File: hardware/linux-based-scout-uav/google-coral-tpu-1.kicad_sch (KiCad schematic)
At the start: 1 part, among them U10 G313-06329-00

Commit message: Schematic and board update
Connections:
- net USB_2_DP: now reaches U10.13 (USB2_D_P)
- net USB_2_DN: now reaches U10.14 (USB2_D_N)
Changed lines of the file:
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@@
+	(wire
+		(pts
+			(xy 168.91 142.24) (xy 180.34 142.24)
+		)
+		(stroke
+			(width 0)
+			(type default)
+		)
+	)
 	(wire
 		(pts
@@
 		)
 	)
+	(wire
+		(pts
+			(xy 168.91 139.7) (xy 180.34 139.7)
+		)
+		(stroke
+			(width 0)
+			(type default)
+		)
+	)
+	(global_label "USB_2_DN"
+		(shape bidirectional)
+		(at 168.91 142.24 180)
+		(fields_autoplaced yes)
+		(effects
+			(font
+				(size 1.27 1.27)
+			)
+			(justify right)
+		)
+		(property "Intersheetrefs" "${INTERSHEET_REFS}"
+			(at 155.2583 142.24 0)
+			(effects
+				(font
+					(size 1.27 1.27)
+				)
+				(justify right)
+				(hide yes)
+			)
+		)
+	)
+	(global_label "USB_2_DP"
+		(shape bidirectional)
+		(at 168.91 139.7 180)
+		(fields_autoplaced yes)
+		(effects
+			(font
+				(size 1.27 1.27)
+			)
+			(justify right)
+		)
+		(property "Intersheetrefs" "${INTERSHEET_REFS}"
+			(at 155.3188 139.7 0)
+			(effects
+				(font
+					(size 1.27 1.27)
+				)
+				(justify right)
+				(hide yes)
+			)
+		)
+	)

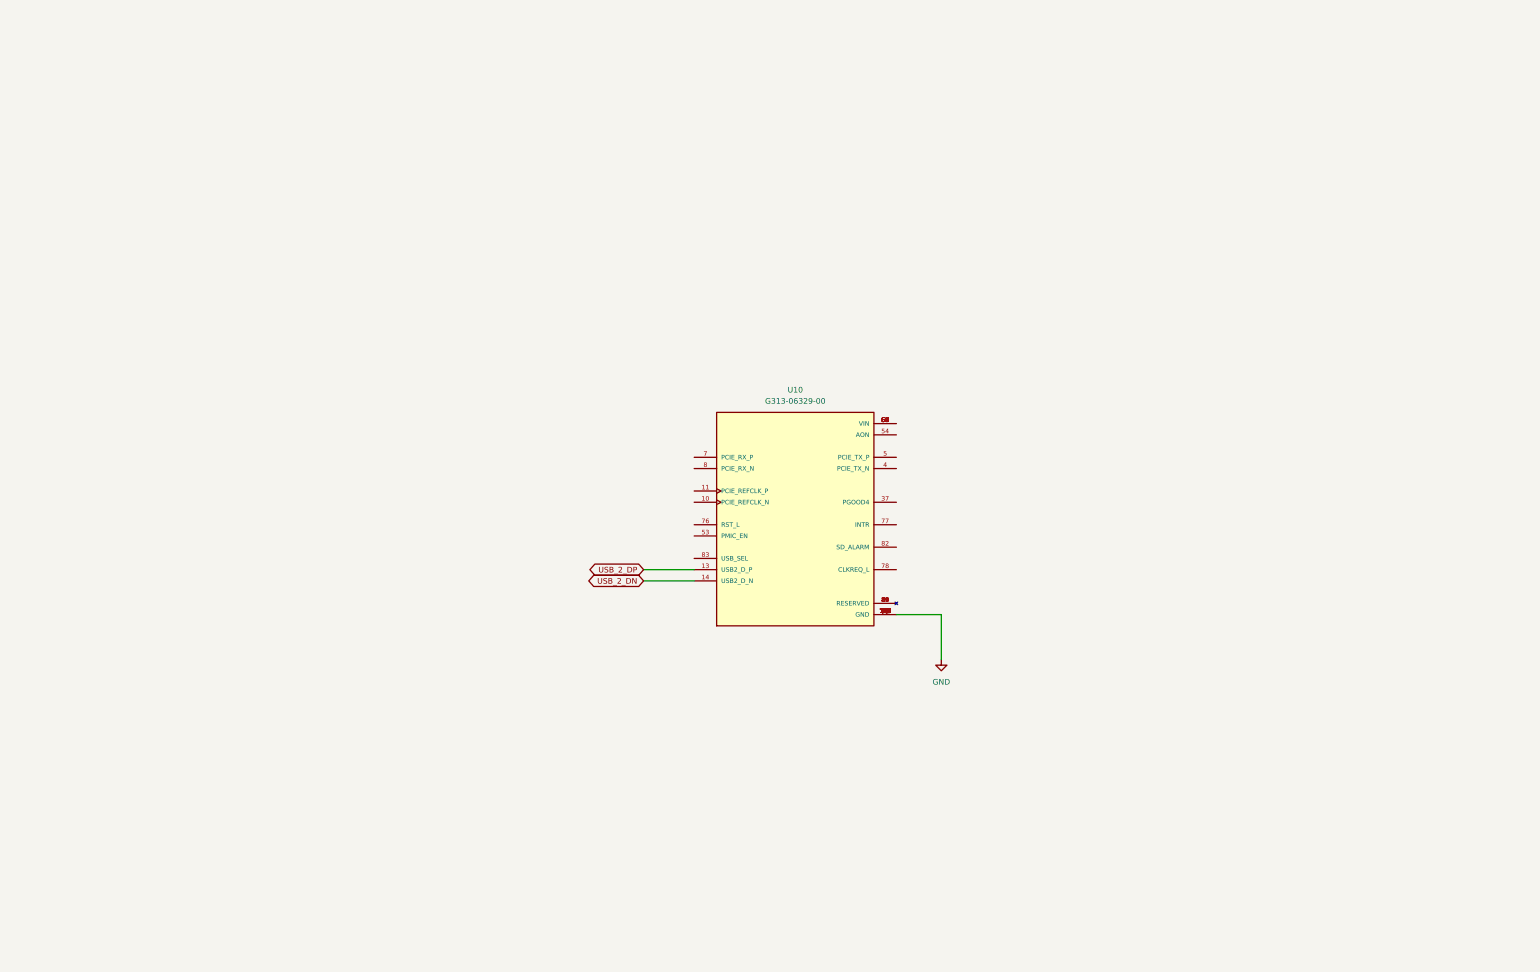
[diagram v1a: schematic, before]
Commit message: Schematic update - added Google Coral
Google Coral edge TPU added to schematic
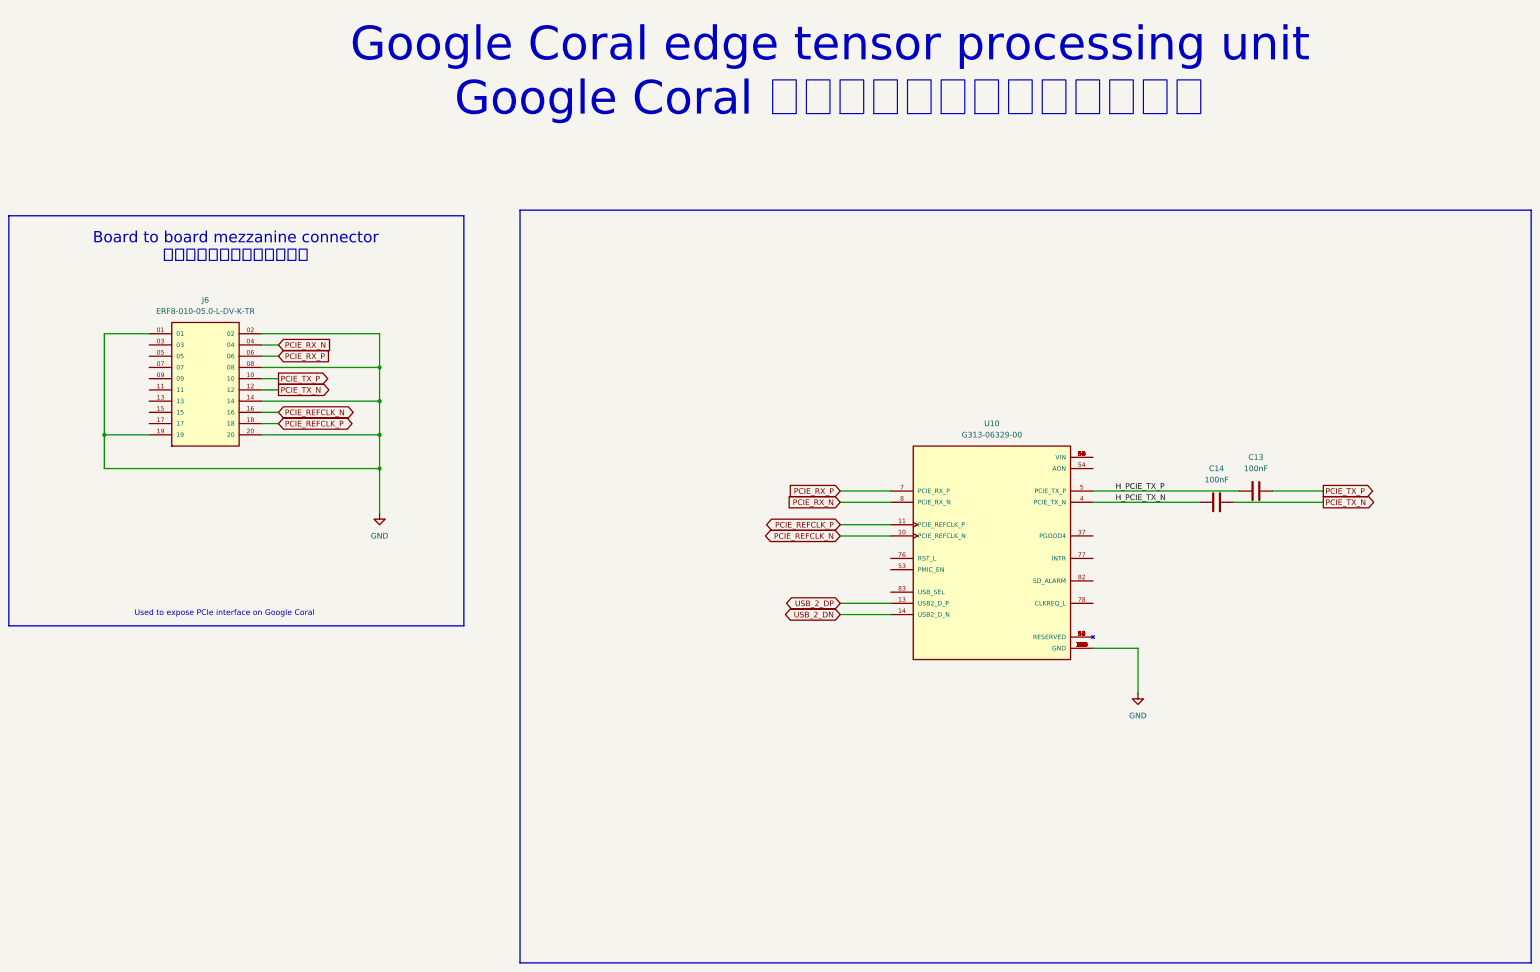
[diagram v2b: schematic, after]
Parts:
- added C13, C14: 100nF, Capacitor_SMD:C_0402_1005Metric, symbol Device:C
- added J6: ERF8-010-05.0-L-DV-K-TR, ERF8-010-05.0-L-DV-K-TR:SAMTEC_ERF8-010-05.0-L-DV-K-TR, symbol ERF8-010-05.0-L-DV-K-TR:ERF8-010-05.0-L-DV-K-TR
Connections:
- net GND: now also J6.01, J6.02, J6.08, J6.14, J6.19, J6.20
- net PCIE_REFCLK_N: now reaches U10.10 (PCIE_REFCLK_N)
- net PCIE_REFCLK_N: now also J6.16
- net PCIE_REFCLK_P: now reaches U10.11 (PCIE_REFCLK_P)
- net PCIE_REFCLK_P: now also J6.18
- net H_PCIE_TX_N: now reaches U10.4 (PCIE_TX_N)
- net H_PCIE_TX_N: now also C14.1
- net H_PCIE_TX_P: now reaches U10.5 (PCIE_TX_P)
- net H_PCIE_TX_P: now also C13.1
- net PCIE_RX_P: now reaches U10.7 (PCIE_RX_P)
- net PCIE_RX_P: now also J6.06
- net PCIE_RX_N: now reaches U10.8 (PCIE_RX_N)
- net PCIE_RX_N: now also J6.04
- new net PCIE_TX_N: C14.2, J6.12
- new net PCIE_TX_P: C13.2, J6.10
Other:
- note added: "Board to board mezzanine connector 基板対基板メザニンコネクタ"
- note added: "Google Coral edge tensor processing unit Google Coral エッジテンソル処理ユニット"
- note added: "Used to expose PCIe interface on Google Coral"
- moved on the sheet: U10

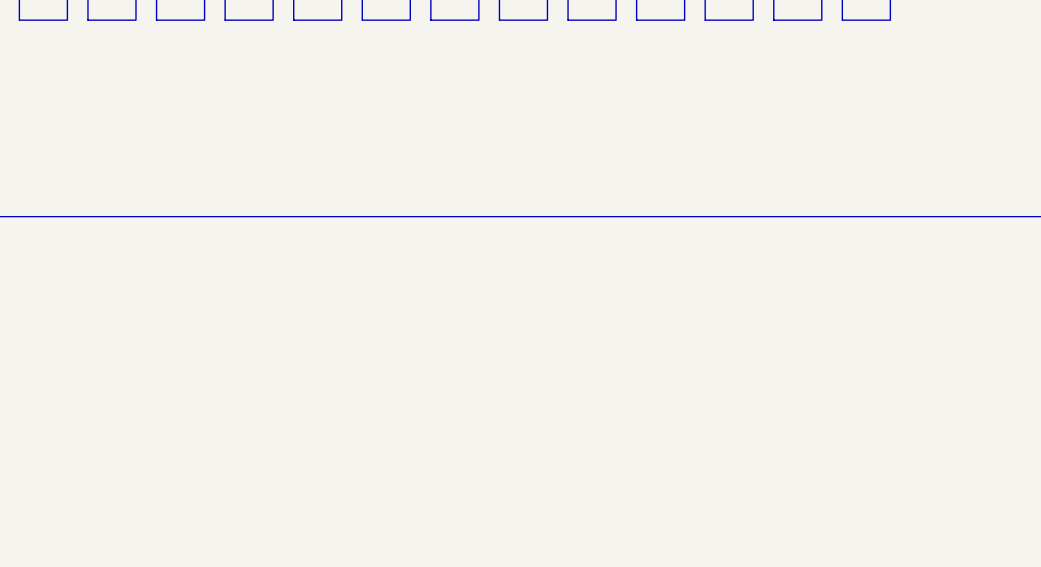
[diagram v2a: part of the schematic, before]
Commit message: Schematic, board update
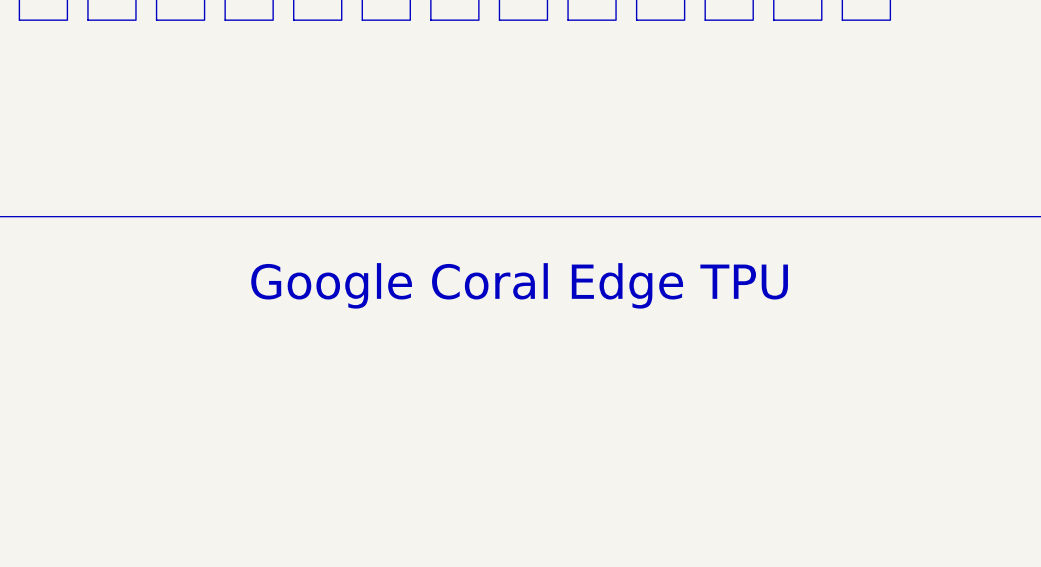
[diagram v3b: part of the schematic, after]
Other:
- note added: "Google Coral Edge TPU"
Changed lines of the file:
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@@
+		)
+	)
+	(text "Google Coral Edge TPU"
+		(exclude_from_sim no)
+		(at 253.746 66.04 0)
+		(effects
+			(font
+				(size 3.81 3.81)
+			)
 		)
 	)
